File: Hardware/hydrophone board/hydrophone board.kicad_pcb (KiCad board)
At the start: 4 copper layers, 147.3 x 66 mm, 163 parts, among them J1 AudioJack3_Ground, J111 Conn_01x02, J121 Conn_01x02, J131 Conn_01x02, J141 Conn_01x02, J2 AudioJack3_Ground, J211 Conn_01x02, J221 Conn_01x02, J231 Conn_01x02, J241 Conn_01x02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

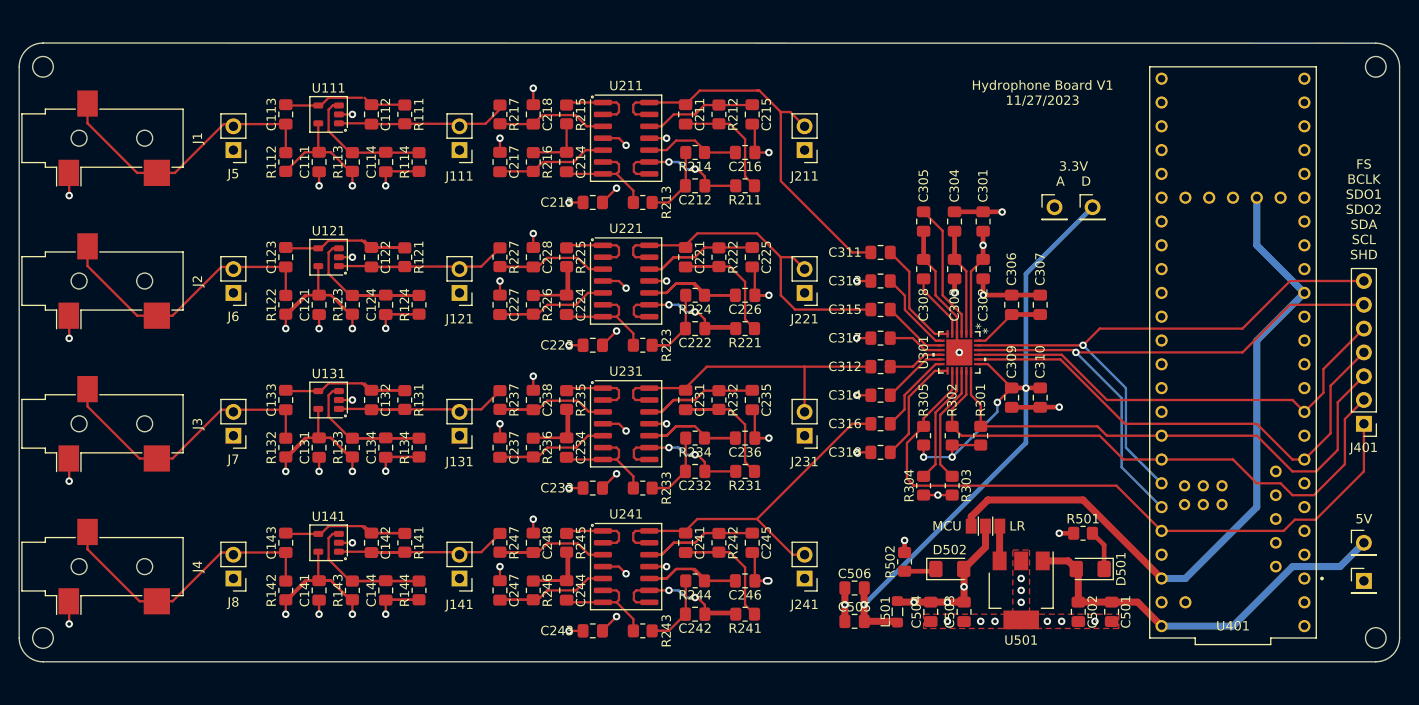
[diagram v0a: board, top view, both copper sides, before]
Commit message: resized board, added 3d model for audio jack
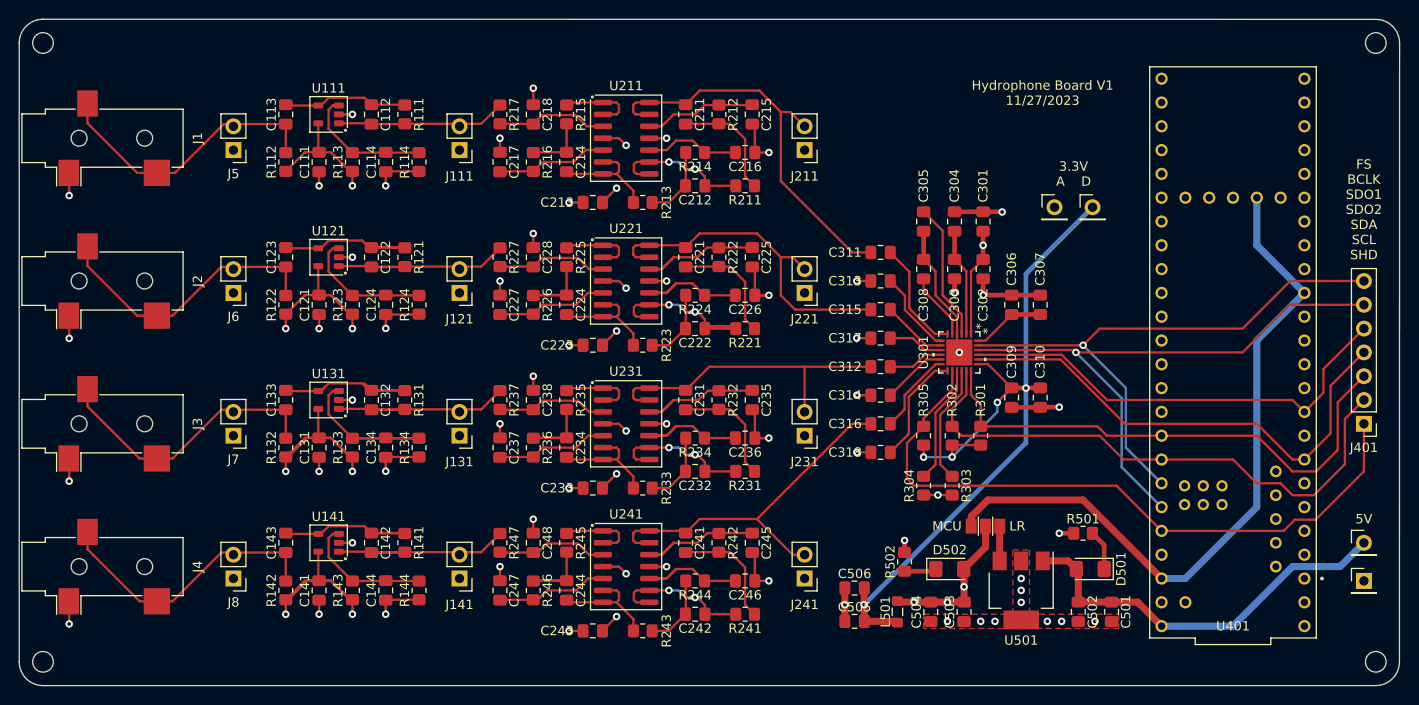
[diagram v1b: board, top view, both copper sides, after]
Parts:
- moved REF** 2.54 mm to (68.6, 35.6)
- moved REF** 2.54 mm to (210.8, 35.6)
- moved REF** 2.54 mm to (210.8, 101.6)
- moved REF** 2.54 mm to (68.6, 101.6)
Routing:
- net GND: track 151.0 -> 139.5 mm, vias 59 -> 58
- net Net-(U221C-+): track 20.3 -> 13.4 mm
- net Net-(U241C-+): track 20.3 -> 13.4 mm
- net Net-(U141-+): track 20.0 -> 13.5 mm
- net Net-(U121-+): track 20.0 -> 13.5 mm
- net Net-(U231C-+): track 18.9 -> 13.4 mm
- net +3.3VA: track 130.0 -> 125.8 mm
- net Net-(U241C--): track 19.3 -> 15.3 mm
- net Net-(U241A-+): track 14.5 -> 11.1 mm
- net Net-(C241-Pad2): track 16.7 -> 13.4 mm
- net Net-(C231-Pad2): track 16.7 -> 13.6 mm
- net Net-(C221-Pad2): track 16.7 -> 13.6 mm
- net Net-(U241B-+): track 14.5 -> 11.4 mm
- net Net-(C234-Pad2): track 12.7 -> 9.88 mm
- net Net-(C244-Pad2): track 12.7 -> 9.88 mm
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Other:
- board size 147.3 x 66 mm -> 147.3 x 71.1 mm

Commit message: resolved all drc errors
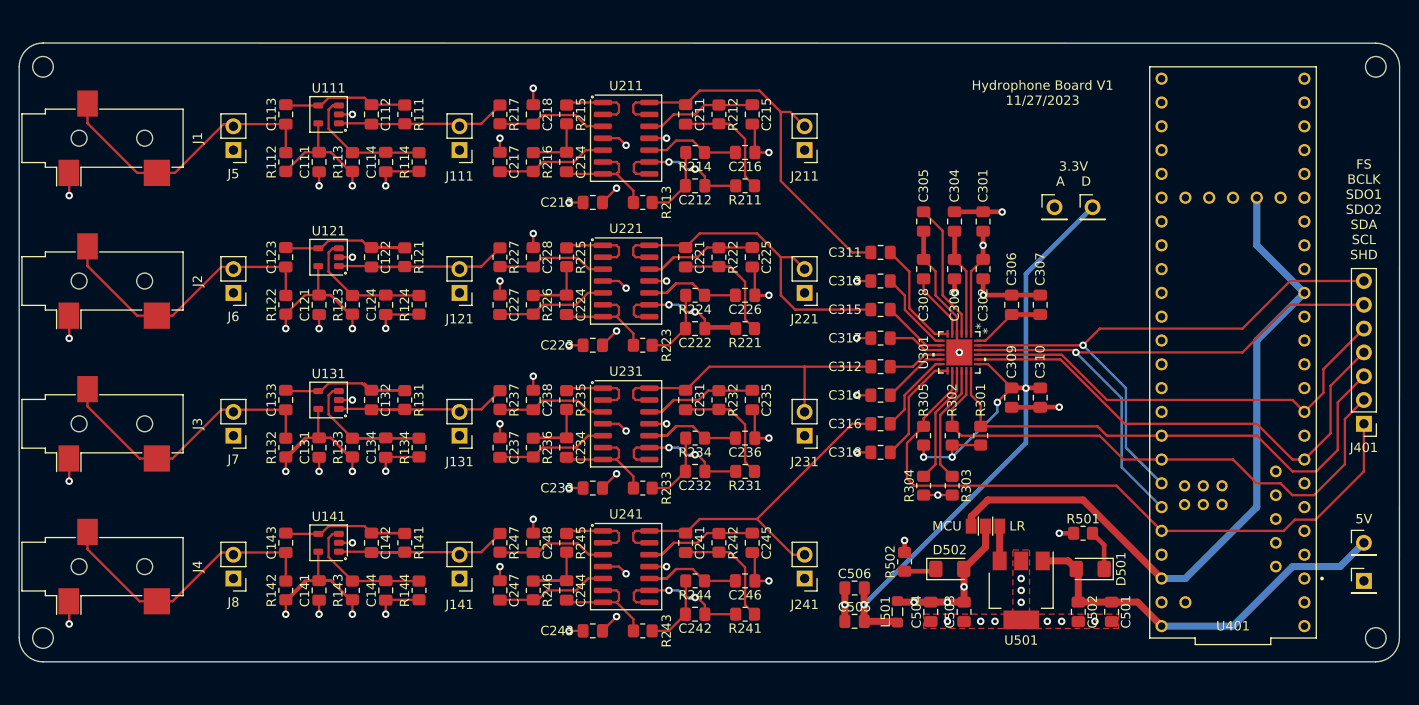
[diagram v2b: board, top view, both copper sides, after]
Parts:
- moved REF** 2.54 mm to (68.6, 38.1)
- moved REF** 2.54 mm to (210.8, 38.1)
- moved REF** 2.54 mm to (210.8, 99.1)
- moved REF** 2.54 mm to (68.6, 99.1)
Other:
- board size 147.3 x 71.1 mm -> 147.3 x 66 mm
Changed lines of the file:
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@@
   )
   (footprint "MountingHole:MountingHole_2.2mm_M2" (layer "F.Cu")
-    (at 210.82 101.6)
+    (at 210.82 99.06)
     (descr "Mounting Hole 2.2mm, no annular, M2")
     (tags "mounting hole 2.2mm no annular m2")
@@
   )
   (footprint "MountingHole:MountingHole_2.2mm_M2" (layer "F.Cu")
-    (at 68.58 35.56)
+    (at 68.58 38.1)
     (descr "Mounting Hole 2.2mm, no annular, M2")
     (tags "mounting hole 2.2mm no annular m2")
@@
     (fp_line (start 3.1 8.6) (end -3.1 8.6)
       (stroke (width 0.12) (type solid)) (layer "F.SilkS"))
-    (fp_line (start -5.6 -9) (end 5.6 -9)
+    (fp_line (start -5.08 -9) (end 5.08 -9)
       (stroke (width 0.05) (type solid)) (layer "F.CrtYd"))
-    (fp_line (start -5.6 9) (end -5.6 -9)
+    (fp_line (start -5.08 9) (end -5.08 -9)
       (stroke (width 0.05) (type solid)) (layer "F.CrtYd"))
-    (fp_line (start 5.6 -9) (end 5.6 9)
+    (fp_line (start 5.08 -9) (end 5.08 9)
       (stroke (width 0.05) (type solid)) (layer "F.CrtYd"))
-    (fp_line (start 5.6 9) (end -5.6 9)
+    (fp_line (start 5.08 9) (end -5.08 9)
       (stroke (width 0.05) (type solid)) (layer "F.CrtYd"))
     (fp_line (start -3 -6) (end -2.5 -6)
@@
       (rotate (xyz 0 0 0))
     )
+    (model "${KIPRJMOD}/library/SJ-3523-SMT-TR/SJ-3523-SMT-TR.step"
+      (offset (xyz 0 2.5 0))
+      (scale (xyz 1 1 1))
+      (rotate (xyz -90 0 90))
+    )
   )
   (footprint "Resistor_SMD:R_0805_2012Metric_Pad1.20x1.40mm_HandSolder" (layer "F.Cu")
@@
     (fp_line (start 3.1 8.6) (end -3.1 8.6)
       (stroke (width 0.12) (type solid)) (layer "F.SilkS"))
-    (fp_line (start -5.6 -9) (end 5.6 -9)
+    (fp_line (start -5.08 -9) (end 5.08 -9)
       (stroke (width 0.05) (type solid)) (layer "F.CrtYd"))
-    (fp_line (start -5.6 9) (end -5.6 -9)
+    (fp_line (start -5.08 9) (end -5.08 -9)
       (stroke (width 0.05) (type solid)) (layer "F.CrtYd"))
-    (fp_line (start 5.6 -9) (end 5.6 9)
+    (fp_line (start 5.08 -9) (end 5.08 9)
       (stroke (width 0.05) (type solid)) (layer "F.CrtYd"))
-    (fp_line (start 5.6 9) (end -5.6 9)
+    (fp_line (start 5.08 9) (end -5.08 9)
       (stroke (width 0.05) (type solid)) (layer "F.CrtYd"))
     (fp_line (start -3 -6) (end -2.5 -6)
@@
       (rotate (xyz 0 0 0))
     )
+    (model "${KIPRJMOD}/library/SJ-3523-SMT-TR/SJ-3523-SMT-TR.step"
+      (offset (xyz 0 2.5 0))
+      (scale (xyz 1 1 1))
+      (rotate (xyz -90 0 90))
+    )
   )
   (footprint "Capacitor_SMD:C_0805_2012Metric_Pad1.18x1.45mm_HandSolder" (layer "F.Cu")
@@
     (fp_line (start 3.1 8.6) (end -3.1 8.6)
       (stroke (width 0.12) (type solid)) (layer "F.SilkS"))
-    (fp_line (start -5.6 -9) (end 5.6 -9)
+    (fp_line (start -5.08 -9) (end 5.08 -9)
       (stroke (width 0.05) (type solid)) (layer "F.CrtYd"))
-    (fp_line (start -5.6 9) (end -5.6 -9)
+    (fp_line (start -5.08 9) (end -5.08 -9)
       (stroke (width 0.05) (type solid)) (layer "F.CrtYd"))
-    (fp_line (start 5.6 -9) (end 5.6 9)
+    (fp_line (start 5.08 -9) (end 5.08 9)
       (stroke (width 0.05) (type solid)) (layer "F.CrtYd"))
-    (fp_line (start 5.6 9) (end -5.6 9)
+    (fp_line (start 5.08 9) (end -5.08 9)
       (stroke (width 0.05) (type solid)) (layer "F.CrtYd"))
     (fp_line (start -3 -6) (end -2.5 -6)
@@
       (rotate (xyz 0 0 0))
     )
+    (model "${KIPRJMOD}/library/SJ-3523-SMT-TR/SJ-3523-SMT-TR.step"
+      (offset (xyz 0 2.5 0))
+      (scale (xyz 1 1 1))
+      (rotate (xyz -90 0 90))
+    )
   )
   (footprint "Resistor_SMD:R_0805_2012Metric_Pad1.20x1.40mm_HandSolder" (layer "F.Cu")
@@
     (fp_line (start 3.1 8.6) (end -3.1 8.6)
       (stroke (width 0.12) (type solid)) (layer "F.SilkS"))
-    (fp_line (start -5.6 -9) (end 5.6 -9)
+    (fp_line (start -5.08 -9) (end 5.08 -9)
       (stroke (width 0.05) (type solid)) (layer "F.CrtYd"))
-    (fp_line (start -5.6 9) (end -5.6 -9)
+    (fp_line (start -5.08 9) (end -5.08 -9)
       (stroke (width 0.05) (type solid)) (layer "F.CrtYd"))
-    (fp_line (start 5.6 -9) (end 5.6 9)
+    (fp_line (start 5.08 -9) (end 5.08 9)
       (stroke (width 0.05) (type solid)) (layer "F.CrtYd"))
-    (fp_line (start 5.6 9) (end -5.6 9)
+    (fp_line (start 5.08 9) (end -5.08 9)
       (stroke (width 0.05) (type solid)) (layer "F.CrtYd"))
     (fp_line (start -3 -6) (end -2.5 -6)
@@
       (rotate (xyz 0 0 0))
     )
+    (model "${KIPRJMOD}/library/SJ-3523-SMT-TR/SJ-3523-SMT-TR.step"
+      (offset (xyz 0 2.5 0))
+      (scale (xyz 1 1 1))
+      (rotate (xyz -90 0 90))
+    )
   )
   (footprint "Resistor_SMD:R_0805_2012Metric_Pad1.20x1.40mm_HandSolder" (layer "F.Cu")
@@
   )
   (footprint "MountingHole:MountingHole_2.2mm_M2" (layer "F.Cu")
-    (at 210.82 35.56)
+    (at 210.82 38.1)
     (descr "Mounting Hole 2.2mm, no annular, M2")
     (tags "mounting hole 2.2mm no annular m2")
@@
   )
   (footprint "MountingHole:MountingHole_2.2mm_M2" (layer "F.Cu")
-    (at 68.58 101.6)
+    (at 68.58 99.06)
     (descr "Mounting Hole 2.2mm, no annular, M2")
     (tags "mounting hole 2.2mm no annular m2")
@@
     )
   )
-  (gr_arc (start 213.341949 101.6) (mid 212.598 103.396051) (end 210.801949 104.14)
+  (gr_arc (start 213.341949 99.06) (mid 212.598 100.856051) (end 210.801949 101.6)
     (stroke (width 0.1) (type default)) (layer "Edge.Cuts"))
-  (gr_arc (start 68.58 104.14) (mid 66.77532 103.387381) (end 66.040118 101.575535)
+  (gr_arc (start 68.58 101.6) (mid 66.77532 100.847381) (end 66.040118 99.035535)
     (stroke (width 0.1) (type default)) (layer "Edge.Cuts"))
-  (gr_line (start 68.58 33.02) (end 210.82 33.038051)
+  (gr_line (start 68.58 35.56) (end 210.82 35.578051)
     (stroke (width 0.1) (type default)) (layer "Edge.Cuts"))
-  (gr_arc (start 66.04 35.56) (mid 66.783949 33.763949) (end 68.58 33.02)
+  (gr_arc (start 66.04 38.1) (mid 66.783949 36.303949) (end 68.58 35.56)
     (stroke (width 0.1) (type default)) (layer "Edge.Cuts"))
-  (gr_arc (start 210.82 33.038051) (mid 212.616051 33.782) (end 213.36 35.578051)
+  (gr_arc (start 210.82 35.578051) (mid 212.616051 36.322) (end 213.36 38.118051)
     (stroke (width 0.1) (type default)) (layer "Edge.Cuts"))
-  (gr_line (start 213.36 35.578051) (end 213.341949 101.6)
+  (gr_line (start 213.36 38.118051) (end 213.341949 99.06)
     (stroke (width 0.1) (type default)) (layer "Edge.Cuts"))
-  (gr_line (start 66.039936 101.575533) (end 66.04 35.56)
+  (gr_line (start 66.040118 99.035535) (end 66.04 38.1)
     (stroke (width 0.1) (type default)) (layer "Edge.Cuts"))
-  (gr_line (start 210.801949 104.14) (end 68.58 104.14)
+  (gr_line (start 210.801949 101.6) (end 68.58 101.6)
     (stroke (width 0.1) (type default)) (layer "Edge.Cuts"))
   (gr_text "3.3V\nA    D" (at 178.562 49.53) (layer "F.SilkS")
@@
   )
   (dimension (type aligned) (layer "User.3")
-    (pts (xy 213.36 33.02) (xy 213.361798 104.14))
+    (pts (xy 213.36 35.56) (xy 213.36 101.6))
     (height -5.104475)
-    (gr_text "2.8000 in" (at 219.615374 68.579842 270.0014485) (layer "User.3")
+    (gr_text "2.6000 in" (at 217.314475 68.58 90) (layer "User.3")
       (effects (font (size 1 1) (thickness 0.15)))
     )
@@
   )
   (dimension (type aligned) (layer "User.3")
-    (pts (xy 66.041798 104.14) (xy 213.361798 104.14))
+    (pts (xy 66.041798 101.6) (xy 213.361798 101.6))
     (height 4.451626)
-    (gr_text "5.8000 in" (at 139.701798 107.441626) (layer "User.3")
+    (gr_text "5.8000 in" (at 139.701798 104.901626) (layer "User.3")
       (effects (font (size 1 1) (thickness 0.15)))
     )
@@
   )
   (dimension (type aligned) (layer "User.3")
-    (pts (xy 210.82 101.6) (xy 210.82 35.56))
+    (pts (xy 210.82 99.06) (xy 210.82 38.1))
     (height 5.08)
-    (gr_text "2.6000 in" (at 214.75 68.58 90) (layer "User.3")
+    (gr_text "2.4000 in" (at 214.75 68.58 90) (layer "User.3")
       (effects (font (size 1 1) (thickness 0.15)))
     )
@@
   )
   (dimension (type aligned) (layer "User.3")
-    (pts (xy 68.58 101.6) (xy 210.82 101.6))
+    (pts (xy 68.58 99.06) (xy 210.82 99.06))
     (height 5.08)
-    (gr_text "5.6000 in" (at 139.7 105.53) (layer "User.3")
+    (gr_text "5.6000 in" (at 139.7 102.99) (layer "User.3")
       (effects (font (size 1 1) (thickness 0.15)))
     )
@@
   )
   (dimension (type radial) (layer "User.3")
-    (pts (xy 210.82 35.578051) (xy 210.82 33.038051))
+    (pts (xy 210.82 38.118051) (xy 210.82 35.578051))
     (leader_length 3.81)
-    (gr_text "R 100.0000 mils" (at 220.726 29.228051) (layer "User.3")
+    (gr_text "R 100.0000 mils" (at 220.726 31.768051) (layer "User.3")
       (effects (font (size 1 1) (thickness 0.15)))
     )

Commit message: resized mounting holes, trace length matching, added logo
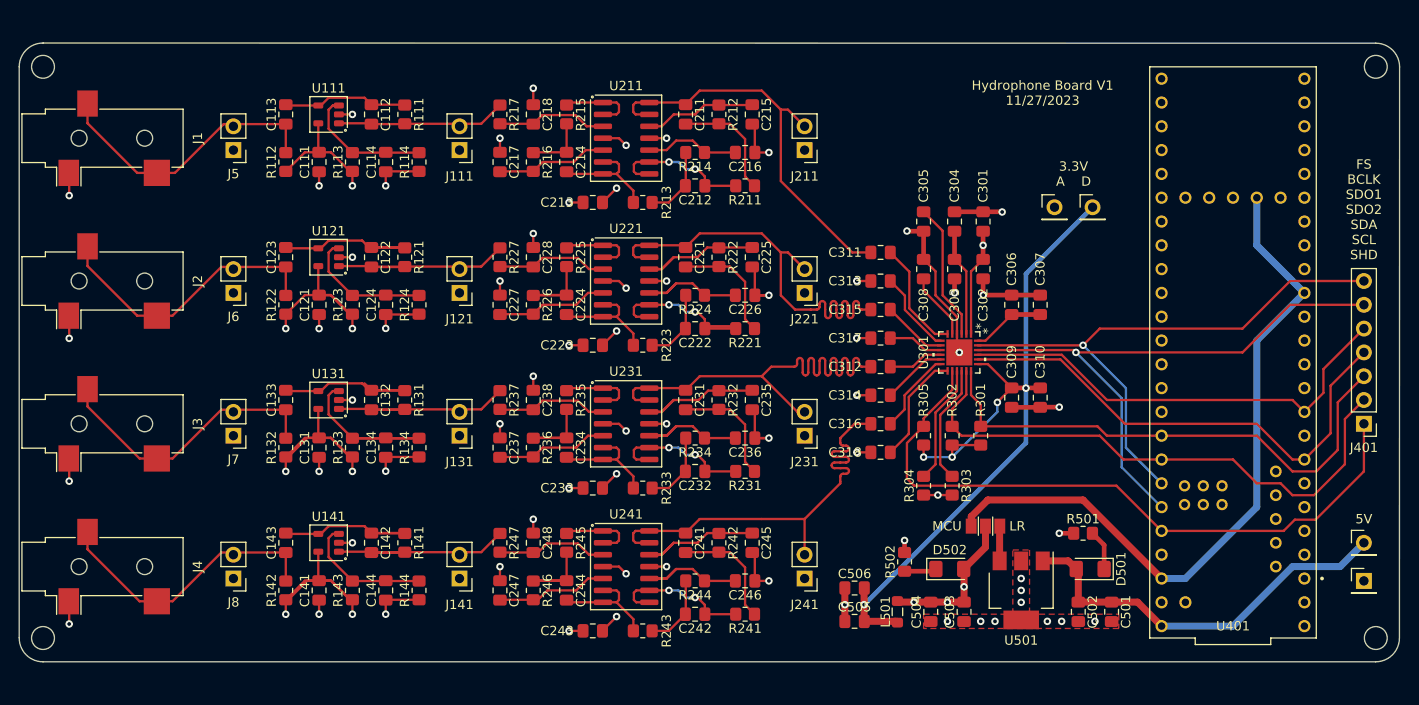
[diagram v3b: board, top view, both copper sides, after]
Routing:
- net /IN_3_B: track 34.0 -> 52.3 mm
- net /IN_2_B: track 37.6 -> 48.5 mm
- net /IN_4_B: track 39.6 -> 48.3 mm
- net GND: track 139.5 -> 141.3 mm, vias 58 -> 59

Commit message: changed pre amp op amp
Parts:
- removed REF** (x4): MountingHole_2.2mm_M2, MountingHole:MountingHole_2.2mm_M2
- added G***: LOGO, LOGO, F.Cu at (168.9, 43.2)
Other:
- board text added: "Hydrophone Board V1 11/29/2023"
- board text removed: "Hydrophone Board V1 11/27/2023"

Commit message: BOM things
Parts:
- added REF**: MountingHole_2.1mm, MountingHole:MountingHole_2.1mm, F.Cu at (210.8, 38.1)
- added REF**: MountingHole_2.1mm, MountingHole:MountingHole_2.1mm, F.Cu at (68.6, 99.1)
- added REF**: MountingHole_2.1mm, MountingHole:MountingHole_2.1mm, F.Cu at (68.6, 38.1)
- added REF**: MountingHole_2.1mm, MountingHole:MountingHole_2.1mm, F.Cu at (210.8, 99.1)
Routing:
- net GND: vias 59 -> 67
